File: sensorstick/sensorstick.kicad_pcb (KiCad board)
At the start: 2 copper layers, 85 x 23 mm, 8 parts, among them J1 U217-04XN-XXR84, U1 ESP32-C3_SUPERMINI, U2 SCD40 CO2 module

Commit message: first draft
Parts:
- U1: value ESP32-C3_SUPERMINI -> XIAO-ESP32-C6-SMD; footprint CustomLibrary:ESP32-C3_SUPERMINI_SMD -> CustomLibrary:XIAO-ESP32C6-SMD
- moved U1 0.75 mm to (77.4, 99.7)
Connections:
- U1 pad 1: /IC2_SDA -> /voltage
- U1 pad 20: unconnected-(U1-GPIO20-Pad20) -> GND
- U1 pad 5: unconnected-(U1-GPIO5-Pad5) -> /IC2_SDA
- U1 pad 6: unconnected-(U1-GPIO6-Pad6) -> /I2C_SCL
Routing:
- net /I2C_SCL: track 68.1 -> 80.3 mm, vias 0 -> 2
- net GND: track 5.03 -> 17.0 mm, vias 24 -> 27
- net /IC2_SDA: track 72.6 -> 84.5 mm, vias 0 -> 2
- net +3.3V: track 78.2 -> 68.5 mm
- net +5V: track 43.1 -> 44.6 mm

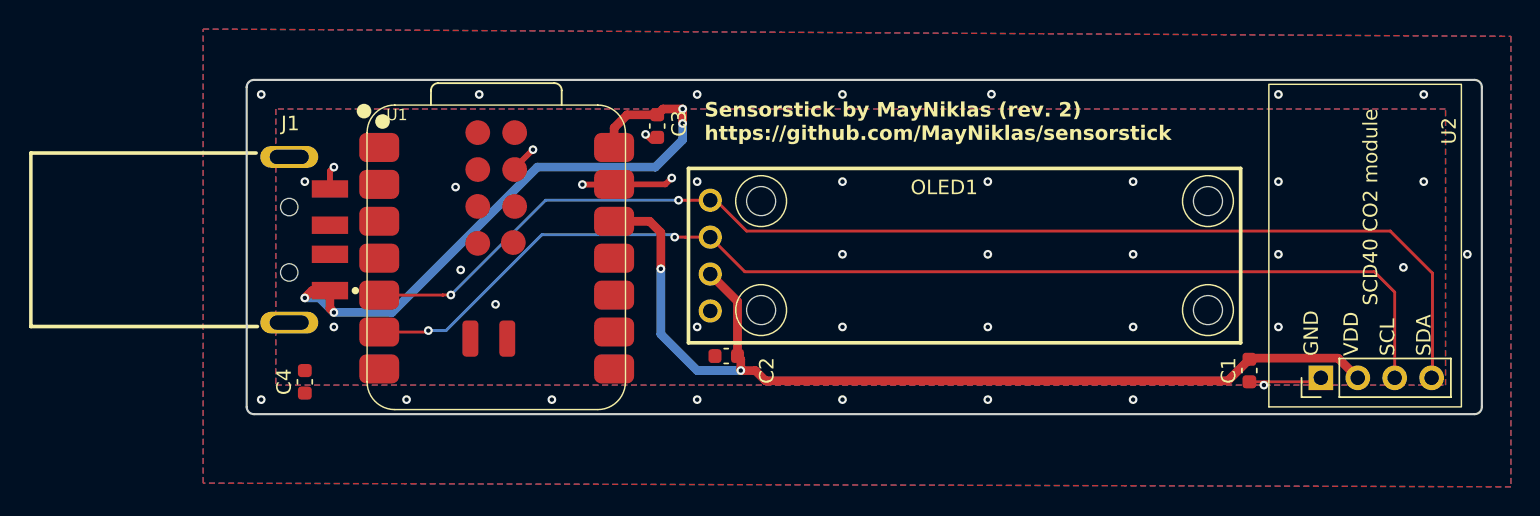
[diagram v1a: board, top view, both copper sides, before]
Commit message: switch to SCD40 chip instead of module
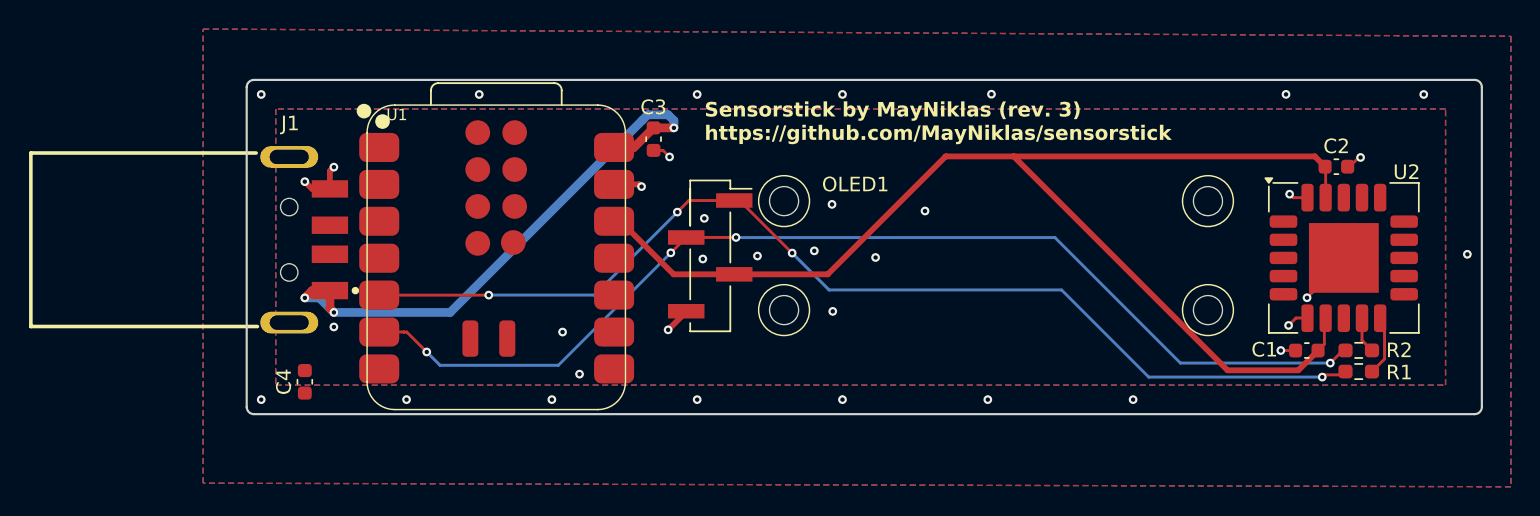
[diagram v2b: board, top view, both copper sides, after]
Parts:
- added R1: 10k, Resistor_SMD:R_0603_1608Metric_Pad0.98x0.95mm_HandSolder, F.Cu at (136.5, 107.6)
- added R2: 10k, Resistor_SMD:R_0603_1608Metric_Pad0.98x0.95mm_HandSolder, F.Cu at (136.5, 106.1)
- OLED1: footprint CustomLibrary:OLED-TH_L38.0-W12.0_HS91L02W2C01 -> CustomLibrary:OLED-TH_L38.0-W12.0_HS91L02W2C01_SMD
- U2: value SCD40 CO2 module -> SCD40-D-R2; footprint CustomLibrary:SCD40_CO2_module -> Sensor:Sensirion_SCD4x-1EP_10.1x10.1mm_P1.25mm_EP4.8x4.8mm
- moved C2 44.0 mm to (135.0, 93.5)
- moved U2 8.53 mm to (135.5, 99.8), turned to 0 degrees
- moved C1 4.19 mm to (133.0, 106.1), turned to 0 degrees
- moved C3 0.93 mm to (88.0, 91.6)
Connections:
- C2 pad 1: +3.3V -> GND
- C2 pad 2: GND -> +3.3V
- U1 pad 1: /voltage -> unconnected-(U1-GPIO0_A0_D0-Pad1)
- U1 pad 15: +BATT -> unconnected-(U1-BAT-Pad15)
- U1 pad 16: -BATT -> unconnected-(U1-GND-Pad16)
- U1 pad 20: GND -> unconnected-(U1-GND-Pad20)
- U2 pad 1: GND -> (no net)
- U2 pad 2: +3.3V -> (no net)
- U2 pad 3: /I2C_SCL -> (no net)
- U2 pad 4: /IC2_SDA -> (no net)
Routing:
- net +3.3V: track 68.5 -> 86.3 mm, vias 2 -> 0
- net /IC2_SDA: track 84.5 -> 74.6 mm, vias 2 -> 4
- net /I2C_SCL: track 80.3 -> 75.2 mm, vias 2 -> 4
- net Net-(U2-SDA): track 0.00 -> 4.15 mm
- net +5V: track 44.6 -> 41.2 mm, vias 4 -> 3
- net Net-(U2-SCL): track 0.00 -> 2.50 mm
- net GND: track 17.0 -> 17.7 mm, vias 27 -> 21
